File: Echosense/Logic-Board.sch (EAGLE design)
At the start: 27 parts, among them IC1 7805T, IC2 1117V33, J1 batt, J2 POWER_JACKPTH_BREAD, J3 Serial, J4 Rotation Sensor, J5 Motor, J6 LIDAR, Q1 45N10, Q3 2N3904

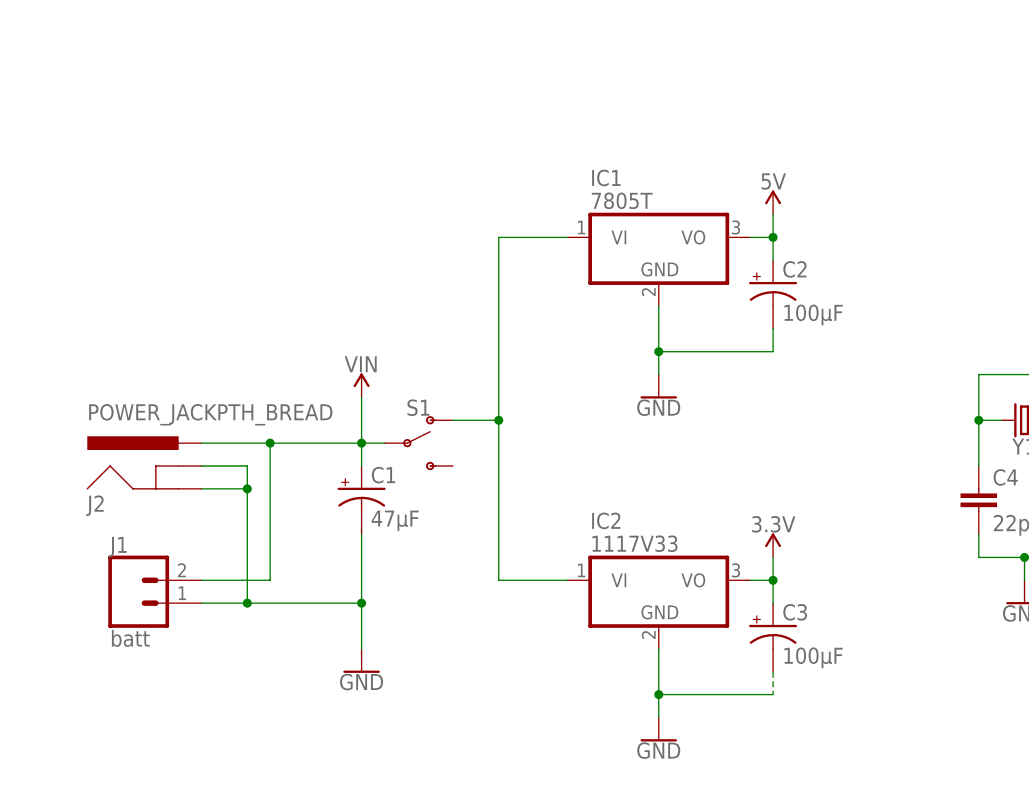
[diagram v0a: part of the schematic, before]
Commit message: Add zener diodes
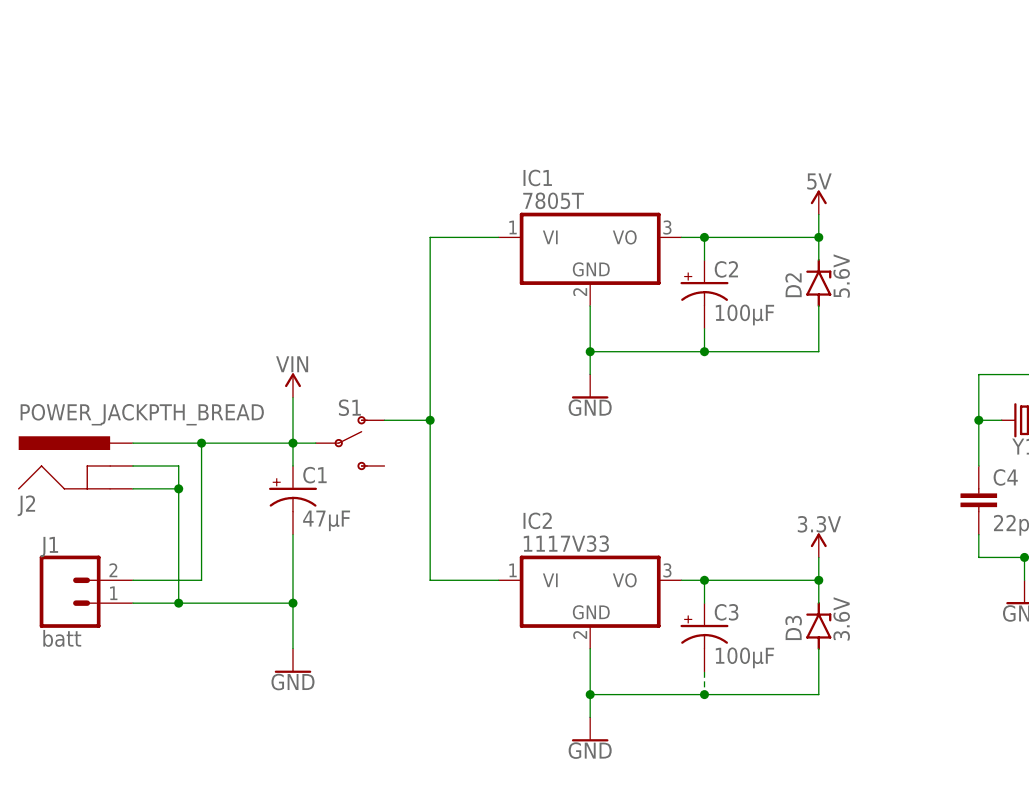
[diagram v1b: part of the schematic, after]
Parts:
- added D2: 5.6V, diode:ZENER-DIODEDO41Z10
- added D3: 3.6V, diode:ZENER-DIODEDO41Z10
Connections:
- net 3.3V: now also D3.C
- net 5V: now also D2.C
- net GND: now also D2.A, D3.A
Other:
- moved on the sheet: C1, C2, C3, IC1, IC2, J1, J2, S1
